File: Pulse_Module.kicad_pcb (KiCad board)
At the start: 2 copper layers, 20.1 x 17.2 mm, 61 parts, among them CON1 AVR-ISP-10, CON2 AVR-JTAG-10, IC1 ATMEGA1280-A, P1 CONN_02X20, P2 USB_OTG, SW1 SW_PUSH, U1 74HCT541_PWR, U2 PL2303, U5 CONN3, U6 WS2812, U7 WS2812, U8 WS2812, U9 CONN3, X1 CRYSTAL, Y1 CRYSTAL

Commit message: Изменения футпринтов и расположения на плате
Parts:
- removed C17: 0.1U, Capacitors_SMD:C_0402
- removed R11: 150, Resistors_SMD:R_0402
- removed the REF** at (87.8, 40.9)
- removed U5: CONN3, Connect:Wafer_Horizontal10x5.8x7RM2.5-3
- removed U9: CONN3, Pin_Headers:Pin_Header_Angled_1x03
- added C16: 0.1uF, Capacitors_SMD:C_0805, F.Cu at (131.8, 89.9)
- added P3: CONN_01X03, Pin_Headers:Pin_Header_Angled_1x03, F.Cu at (165.6, 138.7)
- added P4: CONN_01X03, Pin_Headers:Pin_Header_Angled_1x03, F.Cu at (151.4, 138.7)
- C10, C11, C12, C14, C15, C18, C2, C3, C5, C6, C9: footprint Capacitors_SMD:C_0402 -> Capacitors_SMD:C_0805
- D3: footprint LEDs:LED-8MM -> LEDs:LED_0805
- L1: footprint Inductors:NR4018 -> INDUCTOR-12x12:INDUCTOR_12x12
- R1, R12, R13, R7: footprint Resistors_SMD:R_0805_HandSoldering -> Resistors_ThroughHole:Resistor_Horizontal_RM10mm
- R14, R15, R3, R4, R5, R6: footprint Resistors_SMD:R_0402 -> Resistors_SMD:R_0805
- R2, R8: value 220K -> 220; footprint Resistors_SMD:R_0805_HandSoldering -> Resistors_ThroughHole:Resistor_Horizontal_RM10mm
- U1: footprint Display:HDSP-48xx -> Housings_SSOP:SSOP-20_5.3x7.2mm_Pitch0.65mm
- U6, U7, U8: footprint Connectors_Molex:Connector_Microfit3_Header_02x03_Straight_43045-0628 -> 5050:5050
- moved U1 186.4 mm to (197.9, 95.5)
- moved L1 184.7 mm to (121.9, 135.1), turned to 180 degrees
- moved R14 169.9 mm to (110.2, 129.3)
- moved SW1 166.9 mm to (154.7, 108.0), turned to 90 degrees
- moved R15 160.2 mm to (100.6, 124.7), turned to 180 degrees
- moved C13 112.2 mm to (201.2, 81.8), turned to 90 degrees
- moved C22 107.7 mm to (172.0, 138.2), turned to 180 degrees
- moved C21 97.7 mm to (167.6, 119.4), turned to 180 degrees
- moved U2 80.5 mm to (134.6, 99.8), turned to 90 degrees
- moved C18 76.8 mm to (145.8, 91.9), turned to 90 degrees
- moved C8 72.2 mm to (165.4, 80.5), turned to 90 degrees
- moved REF** 61.0 mm to (273.1, 62.2)
- moved C10 60.9 mm to (166.6, 114.0), turned to 180 degrees
- moved Y1 58.3 mm to (126.5, 79.8), turned to 0 degrees
- moved C15 55.6 mm to (139.4, 89.9), turned to 90 degrees
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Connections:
- IC1 pad 35: Net-(IC1-Pad35) -> /Sheet56DEE0DD/17
- IC1 pad 36: Net-(IC1-Pad36) -> /Sheet56DEE0DD/35
- IC1 pad 37: Net-(IC1-Pad37) -> /Sheet56DEE0DD/36
- IC1 pad 38: Net-(IC1-Pad38) -> /Sheet56DEE0DD/37
- IC1 pad 39: Net-(IC1-Pad39) -> /Sheet56DEE0DD/39
- IC1 pad 40: Net-(IC1-Pad40) -> /Sheet56DEE0DD/34
- IC1 pad 41: Net-(IC1-Pad41) -> /Sheet56DEE0DD/38
- IC1 pad 42: Net-(IC1-Pad42) -> /Sheet56DEE0DD/40
- IC1 pad 84: /Sheet56DEE0DD/34 -> Net-(IC1-Pad84)
- IC1 pad 85: /Sheet56DEE0DD/27 -> Net-(IC1-Pad85)
- IC1 pad 86: /Sheet56DEE0DD/25 -> Net-(IC1-Pad86)
- IC1 pad 87: /Sheet56DEE0DD/23 -> Net-(IC1-Pad87)
- IC1 pad 88: /Sheet56DEE0DD/21 -> Net-(IC1-Pad88)
- IC1 pad 89: /Sheet56DEE0DD/17 -> Net-(IC1-Pad89)
- IC1 pad 96: Net-(IC1-Pad96) -> /Sheet56DEE0DD/CE2
- IC1 pad 97: Net-(IC1-Pad97) -> /Sheet56DEE0DD/CE1
- P1 pad 17: /Sheet56DEE0DD/17 -> /Sheet56DEE0DD/CS
- P1 pad 21: /Sheet56DEE0DD/21 -> /Sheet56DEE0DD/Dout
- P1 pad 23: /Sheet56DEE0DD/23 -> /Sheet56DEE0DD/CLK
- P1 pad 25: /Sheet56DEE0DD/25 -> /Sheet56DEE0DD/CE2
- P1 pad 27: /Sheet56DEE0DD/27 -> /Sheet56DEE0DD/CE1
- P1 pad 29: /Sheet56DEE0DD/CLK -> /Sheet56DEE0DD/CE
- P1 pad 31: /Sheet56DEE0DD/Dout -> /Sheet56DEE0DD/WR
- P1 pad 33: /Sheet56DEE0DD/CS -> /Sheet56DEE0DD/RD
- P1 pad 35: /Sheet56DEE0DD/WR -> /Sheet56DEE0DD/35
- P1 pad 36: /Sheet56DEE0DD/CE2 -> /Sheet56DEE0DD/36
- P1 pad 37: /Sheet56DEE0DD/CE -> /Sheet56DEE0DD/37
- P1 pad 38: GND -> /Sheet56DEE0DD/38
- P1 pad 39: /Sheet56DEE0DD/RD -> /Sheet56DEE0DD/39
- P1 pad 40: GND -> /Sheet56DEE0DD/40
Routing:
- net /Sheet56DEE0DD/35: track 0.00 -> 80.2 mm, vias 0 -> 2
- net /Sheet56DEE0DD/36: track 0.00 -> 62.9 mm, vias 0 -> 2
- net /Sheet56DEE0DD/CE: track 0.00 -> 62.1 mm, vias 0 -> 4
- net /Sheet56DEE0DD/37: track 0.00 -> 59.9 mm, vias 0 -> 4
- net /Sheet56DEE0DD/A15: track 0.00 -> 59.5 mm, vias 0 -> 2
- net /Sheet56DEE0DD/Dout: track 0.00 -> 58.9 mm, vias 0 -> 4
- net /Sheet56DEE0DD/39: track 0.00 -> 56.5 mm, vias 0 -> 2
- net /Sheet56DEE0DD/38: track 0.00 -> 56.1 mm, vias 0 -> 2
- net /Sheet56DEE0DD/34: track 0.00 -> 54.6 mm, vias 0 -> 2
- net /Sheet56DEE0DD/CS: track 0.00 -> 54.2 mm, vias 0 -> 2
- net /Sheet56DEE0DD/A14: track 0.00 -> 52.7 mm, vias 0 -> 4
- net /Sheet56DEE0DD/A13: track 0.00 -> 46.3 mm
- net /Sheet56DEE0DD/CLK: track 0.00 -> 43.7 mm, vias 0 -> 2
- net /Sheet56DEE0DD/RD: track 0.00 -> 43.2 mm
- net /Sheet56DEE0DD/WR: track 0.00 -> 42.6 mm, vias 0 -> 2
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- removed copper zone on F.Cu, net GND
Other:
- board outline removed
- net class Default: clearance 0.2 -> 0.1
- rule trace_clearance: 0.2 -> 0.1
- rule trace_min: 0.2 -> 0.1

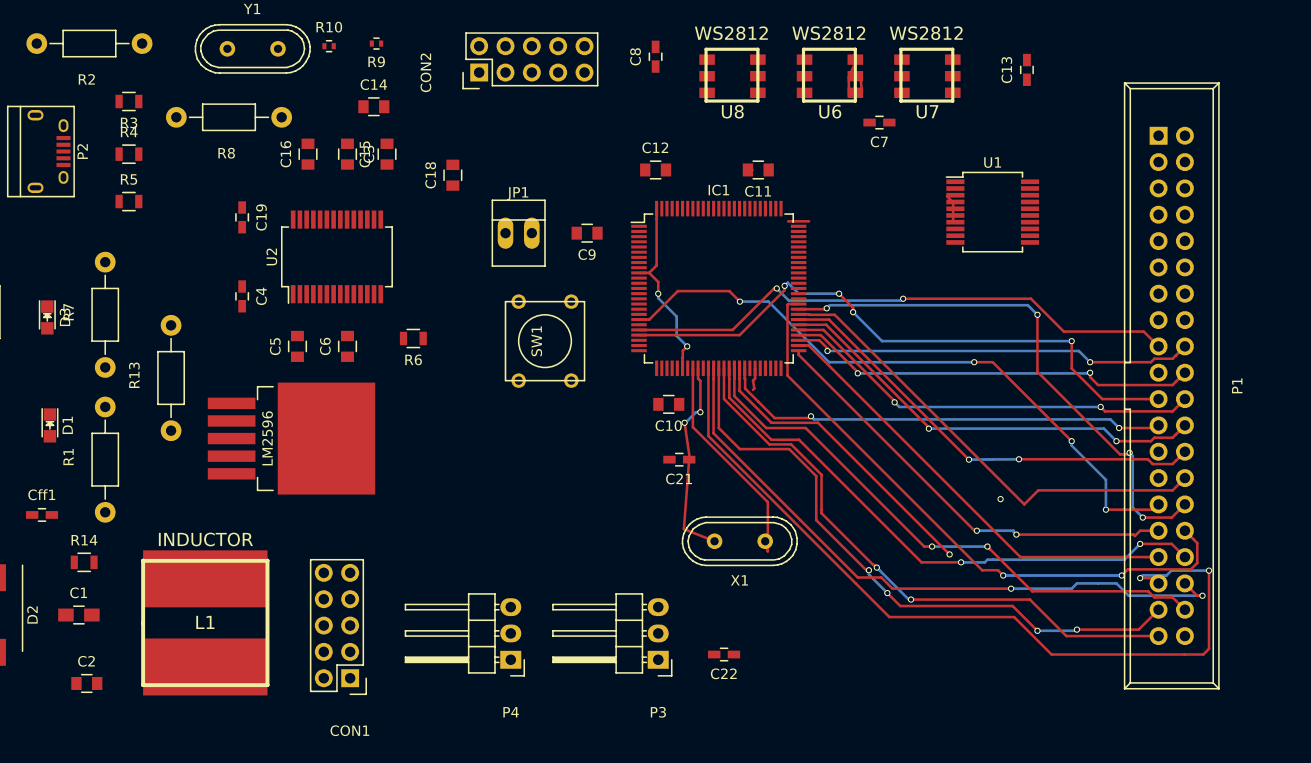
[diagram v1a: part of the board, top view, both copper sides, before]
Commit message: разводка питания
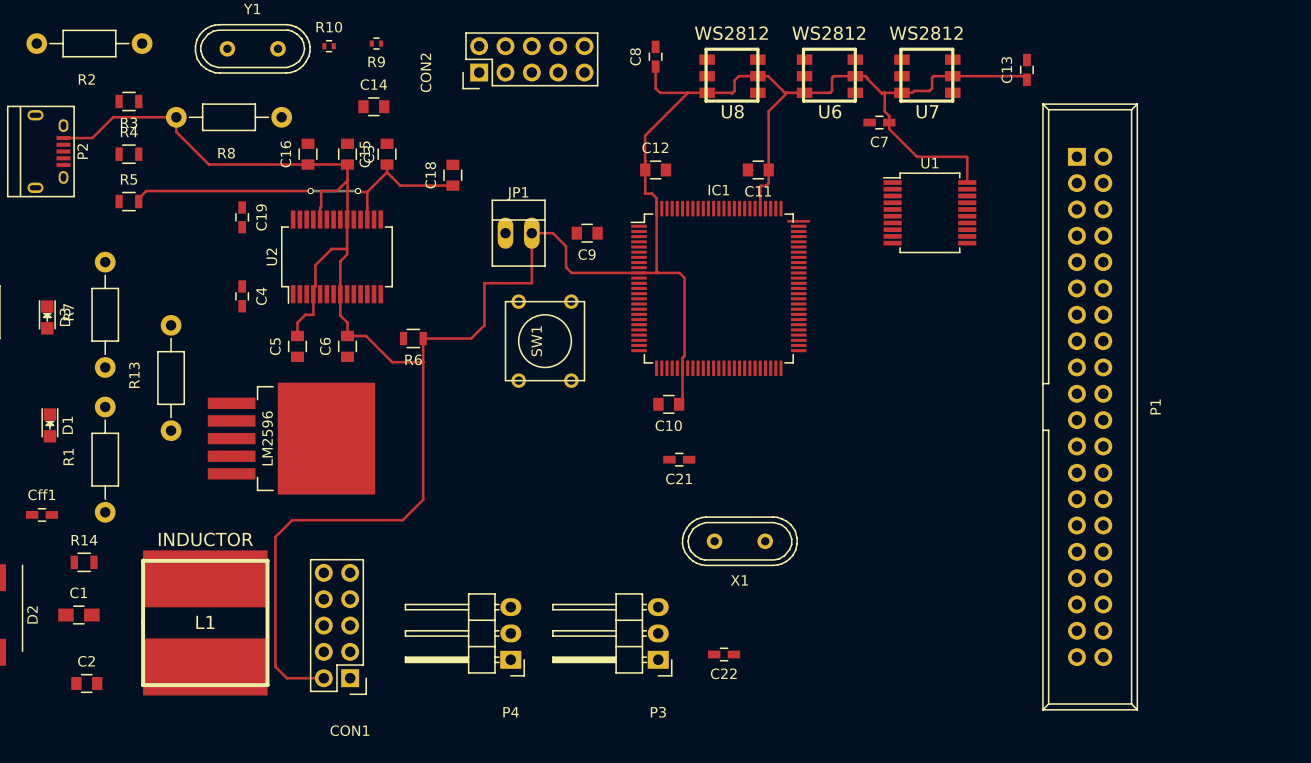
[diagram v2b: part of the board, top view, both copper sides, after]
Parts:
- moved P1 8.13 mm to (206.0, 90.2)
- moved U1 6.05 mm to (191.8, 95.6)
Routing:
- net +5V: track 21.8 -> 264.0 mm, vias 2 -> 0
- net /Sheet56DEE0DD/35: track 80.2 -> 0.00 mm, vias 2 -> 0
- net /Sheet56DEE0DD/36: track 62.9 -> 0.00 mm, vias 2 -> 0
- net /Sheet56DEE0DD/CE: track 62.1 -> 0.00 mm, vias 4 -> 0
- net /Sheet56DEE0DD/37: track 59.9 -> 0.00 mm, vias 4 -> 0
- net /Sheet56DEE0DD/A15: track 59.5 -> 0.00 mm, vias 2 -> 0
- net /Sheet56DEE0DD/Dout: track 58.9 -> 0.00 mm, vias 4 -> 0
- net /Sheet56DEE0DD/39: track 56.5 -> 0.00 mm, vias 2 -> 0
- net /Sheet56DEE0DD/38: track 56.1 -> 0.00 mm, vias 2 -> 0
- net /Sheet56DEE0DD/34: track 54.6 -> 0.00 mm, vias 2 -> 0
- net /Sheet56DEE0DD/CS: track 54.2 -> 0.00 mm, vias 2 -> 0
- net /Sheet56DEE0DD/A14: track 52.7 -> 0.00 mm, vias 4 -> 0
- net /Sheet56DEE0DD/A13: track 46.3 -> 0.00 mm
- net /Sheet56DEE0DD/CLK: track 43.7 -> 0.00 mm, vias 2 -> 0
- net /Sheet56DEE0DD/A12: track 43.6 -> 0.00 mm, vias 2 -> 0
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
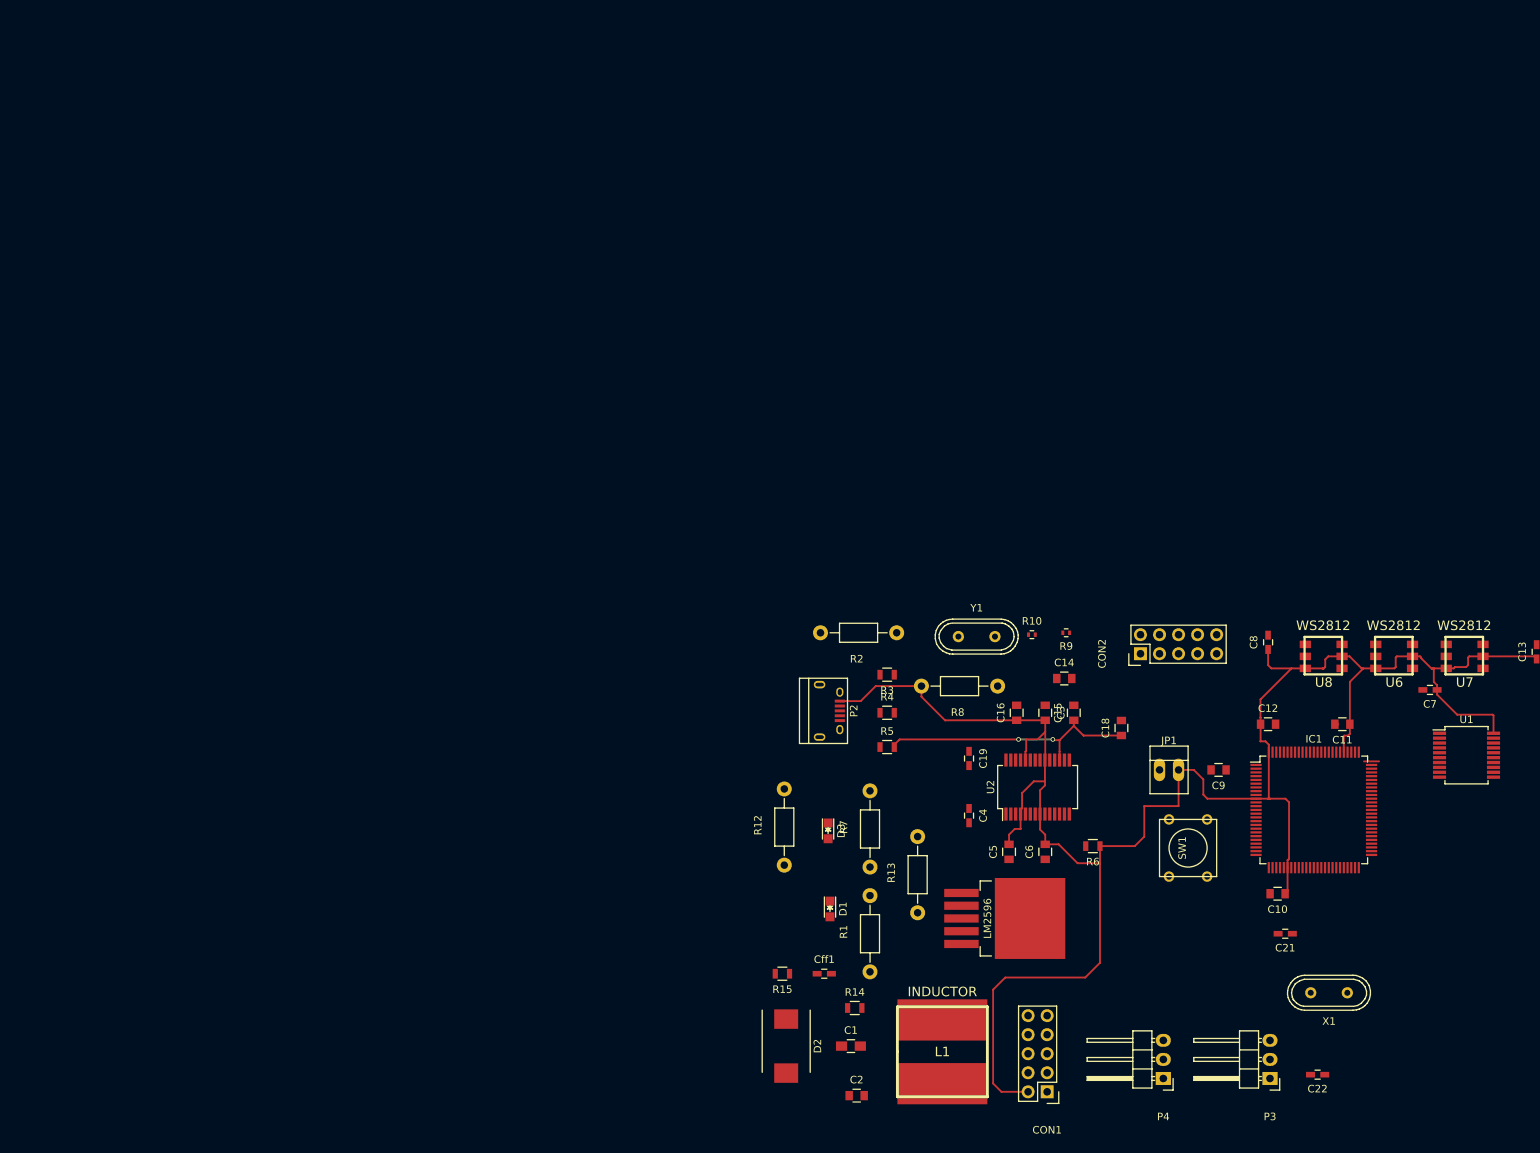
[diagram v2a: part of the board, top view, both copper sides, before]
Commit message: Разведено LM2596
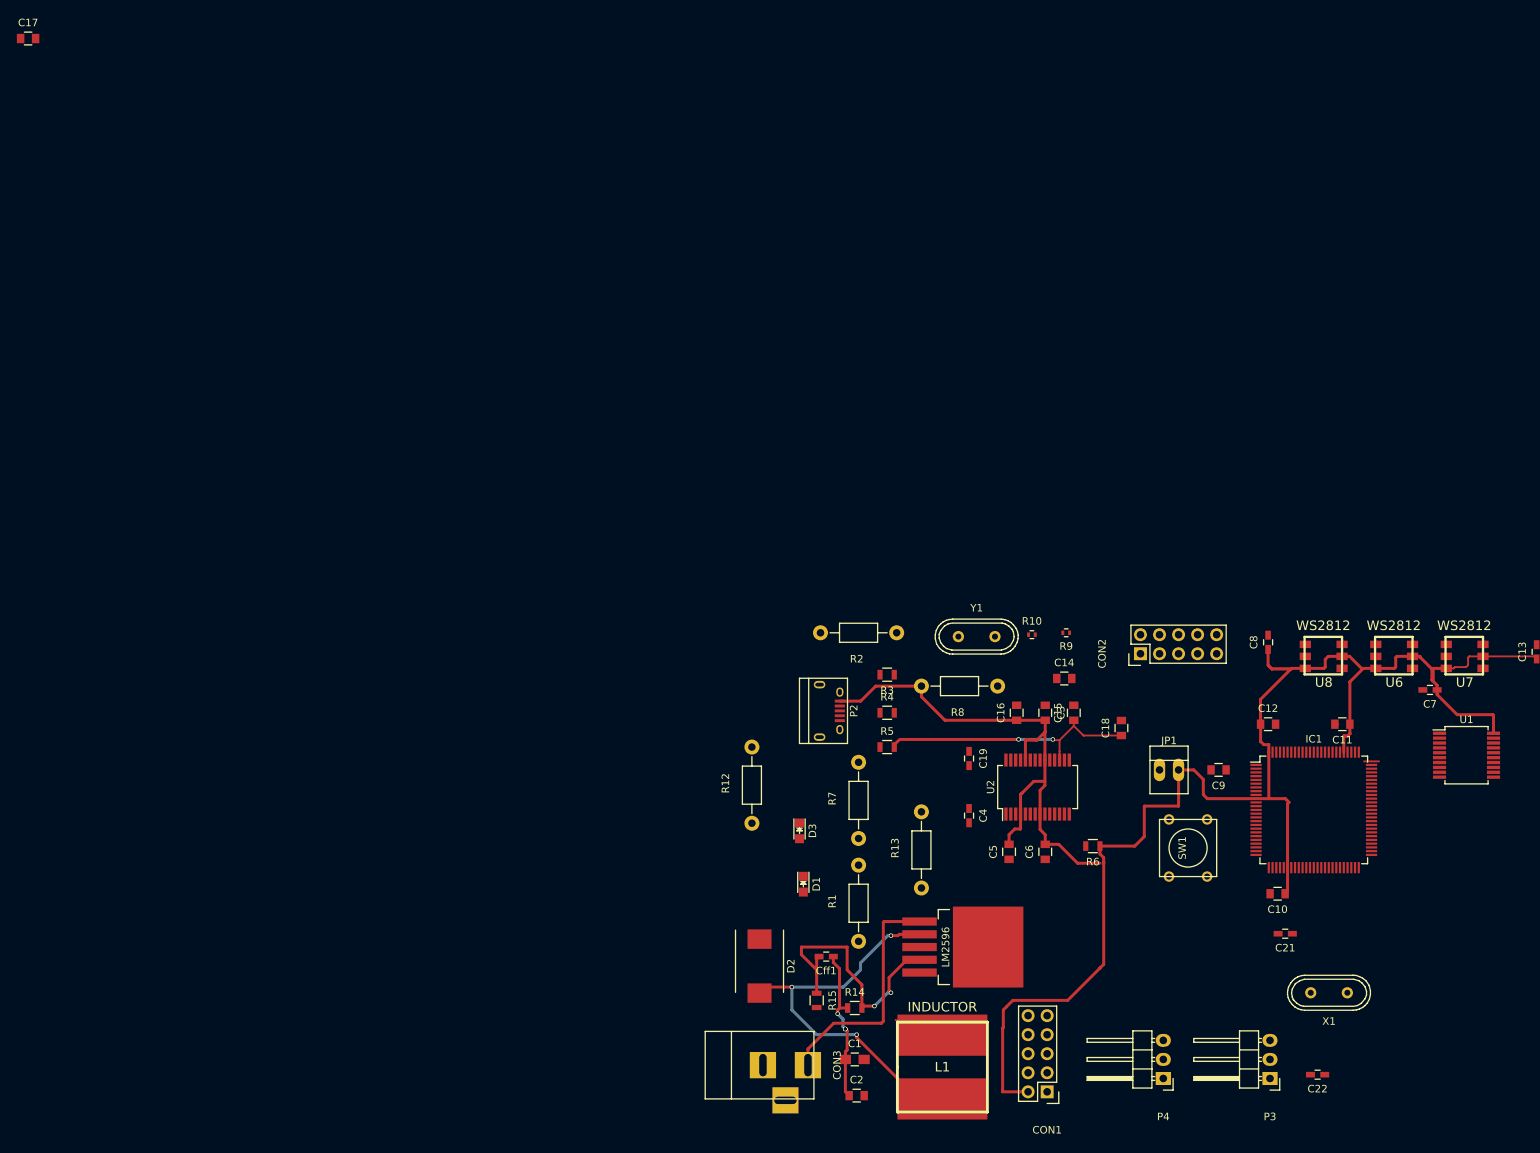
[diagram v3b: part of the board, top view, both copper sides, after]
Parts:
- added C17: 0.1U, Capacitors_SMD:C_0805, F.Cu at (0.00, 0.00)
- added CON3: BARREL_JACK, Connect:BARREL_JACK, F.Cu at (97.8, 136.9)
- moved D2 11.2 mm to (97.5, 123.7)
- moved R12 7.06 mm to (96.5, 104.6)
- moved LM2596 6.76 mm to (118.9, 121.2)
- moved R15 5.79 mm to (105.2, 128.3), turned to 270 degrees
- moved D1 4.85 mm to (103.4, 112.8)
- moved R1 4.34 mm to (110.7, 120.4)
- moved R7 4.10 mm to (110.7, 106.7)
- moved D3 3.81 mm to (102.9, 105.7)
- moved R13 3.34 mm to (119.1, 113.3)
- moved Cff1 2.30 mm to (106.4, 122.4), turned to 180 degrees
- moved L1 2.03 mm to (121.9, 137.2)
- moved C1 1.85 mm to (110.2, 136.1)
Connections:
- LM2596 pad 5: /Sheet56D88A8D/CS -> GND
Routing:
- net Net-(D2-Pad2): track 0.00 -> 53.4 mm, vias 0 -> 3
- net /Sheet56D88A8D/FB: track 0.00 -> 38.2 mm, vias 0 -> 2
- net /Sheet56D88A8D/Vin: track 0.00 -> 31.8 mm
- net /Vcc: track 0.00 -> 27.5 mm, vias 0 -> 3
- net +5V: track 264.0 -> 290.7 mm

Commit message: Питание и LM2596
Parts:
- removed C17: 0.1U, Capacitors_SMD:C_0805
- added JP2: JUMPER, Connect:PINHEAD1-2, F.Cu at (138.7, 113.8)
- C1: footprint Capacitors_SMD:C_0805_HandSoldering -> Capacitors_ThroughHole:C_Radial_D7.5_L11.2_P2.5
- C13, C19, C21, C22, C4, C7, C8: footprint Capacitors_SMD:C_0603_HandSoldering -> Capacitors_SMD:C_0805
- Cff1: footprint Capacitors_SMD:C_0603_HandSoldering -> Capacitors_ThroughHole:C_Radial_D6.3_L11.2_P2.5
- R1, R12, R13, R2, R7, R8: footprint Resistors_ThroughHole:Resistor_Horizontal_RM10mm -> Resistors_SMD:R_0805
- R9: value 150 -> R; footprint Resistors_SMD:R_0402 -> Resistors_SMD:R_0805
- moved R9 40.6 mm to (134.1, 119.6)
- moved Cff1 29.8 mm to (135.9, 127.0)
- moved R12 22.6 mm to (119.1, 103.4)
- moved R15 19.3 mm to (124.5, 127.5)
- moved D2 17.3 mm to (114.8, 124.0)
- moved R14 16.9 mm to (127.0, 127.5), turned to 90 degrees
- moved R7 8.08 mm to (104.9, 112.3), turned to 270 degrees
- moved D3 7.50 mm to (99.3, 112.3)
- moved D1 6.97 mm to (99.6, 118.6)
- moved LM2596 6.53 mm to (125.2, 122.7), turned to 90 degrees
- moved CON3 6.35 mm to (101.6, 131.8), turned to 90 degrees
- moved R1 6.11 mm to (104.9, 118.6), turned to 270 degrees
- moved CON1 3.82 mm to (136.1, 144.3)
- moved C14 3.42 mm to (135.9, 87.9)
- moved C2 3.14 mm to (111.3, 144.0)
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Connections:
- R9 pad 2: +5V -> GND
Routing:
- net +5V: track 290.7 -> 242.8 mm
- net /Vcc: track 27.5 -> 57.8 mm, vias 3 -> 0
- net Net-(D2-Pad2): track 53.4 -> 27.6 mm
- net /Sheet56D88A8D/FB: track 38.2 -> 24.0 mm, vias 2 -> 0
- net Net-(JP2-Pad2): track 0.00 -> 9.81 mm
- net GND: track 0.30 -> 1.59 mm
- net /Sheet56D88A8D/Vin: track 31.8 -> 33.1 mm
- net +3V3: track 35.7 -> 34.4 mm

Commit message: исправления
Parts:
- Cff1: footprint Capacitors_ThroughHole:C_Radial_D6.3_L11.2_P2.5 -> Capacitors_SMD:C_0805
- moved JP2 6.55 mm to (134.9, 119.1)
- moved Cff1 5.14 mm to (130.8, 127.8), turned to 90 degrees
- moved R9 5.00 mm to (136.1, 124.2)
- moved C1 2.54 mm to (112.8, 136.1), turned to 180 degrees
- turned C2 to 180 degrees
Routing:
- net /Vcc: track 57.8 -> 47.2 mm
- net /Sheet56D88A8D/FB: track 24.0 -> 21.9 mm
- net Net-(JP2-Pad2): track 9.81 -> 7.98 mm
- net Net-(D2-Pad2): track 27.6 -> 27.0 mm
